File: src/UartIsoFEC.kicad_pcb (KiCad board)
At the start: 2 copper layers, 24 x 27.9 mm, 34 parts, among them J1 B3B-XH-A, P1 105444-0001, Q1 DMP3099L-13, U1 FT230XS, U2 ADUM5211

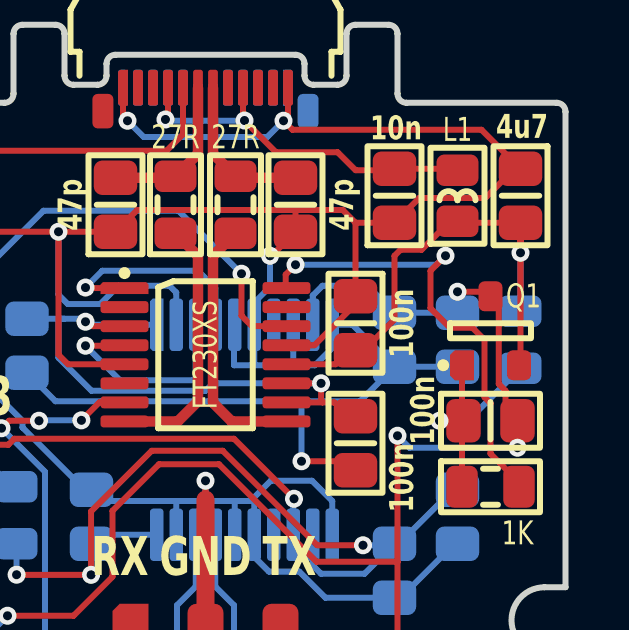
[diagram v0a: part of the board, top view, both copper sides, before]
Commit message: Minor cleanup and expanding soldermask
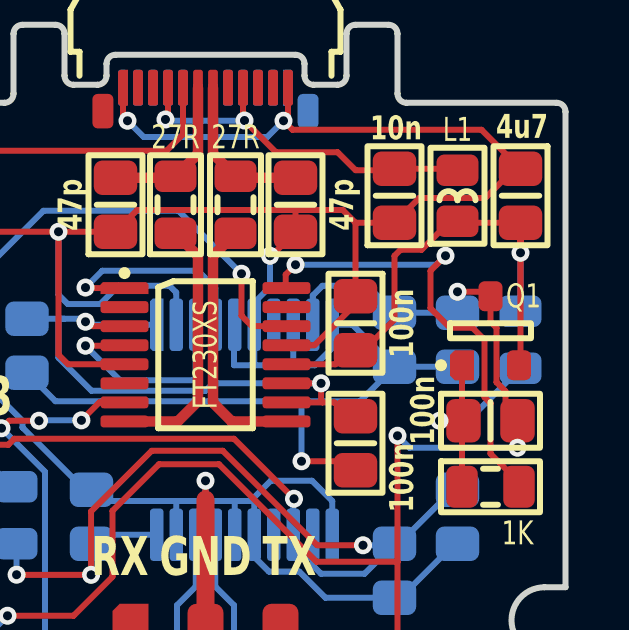
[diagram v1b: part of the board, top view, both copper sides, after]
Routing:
- net GND: track 94.2 -> 93.7 mm
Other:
- rule pad_to_mask_clearance: 0 -> 0.05
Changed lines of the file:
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@@
       (dielectric_constraints no)
     )
-    (pad_to_mask_clearance 0)
+    (pad_to_mask_clearance 0.05)
     (aux_axis_origin 20 20)
     (grid_origin 20 20)
@@
         (effects (font (size 0.8 0.6) (thickness 0.15)))
     )
+    (fp_text user "G" (at -0.95 0.5) (layer "Cmts.User" knockout)
+        (effects (font (size 0.13 0.07) (thickness 0.01) bold))
+    )
+    (fp_text user "D" (at 0 -0.5) (layer "Cmts.User" knockout)
+        (effects (font (size 0.13 0.07) (thickness 0.01) bold))
+    )
     (fp_text user "S" (at 0.95 0.5) (layer "Cmts.User" knockout)
         (effects (font (size 0.13 0.07) (thickness 0.01) bold))
     )
-    (fp_text user "G" (at -0.95 0.5) (layer "Cmts.User" knockout)
-        (effects (font (size 0.13 0.07) (thickness 0.01) bold))
-    )
-    (fp_text user "D" (at 0 -0.5) (layer "Cmts.User" knockout)
-        (effects (font (size 0.13 0.07) (thickness 0.01) bold))
-    )
     (fp_rect (start -1.35 -0.25) (end 1.35 0.25)
       (stroke (width 0.2) (type default)) (fill none) (layer "F.SilkS"))
-    (fp_circle (center -1.575 1.15) (end -1.425 1.15)
+    (fp_circle (center -1.65 1.15) (end -1.5 1.15)
       (stroke (width 0.1) (type solid)) (fill solid) (layer "F.SilkS"))
     (fp_rect (start -1.75 -1.95) (end 1.75 1.95)
@@
   (segment (start 29.4 23.2) (end 29.942136 23.742136) (width 0.2) (layer "B.Cu") (net 1))
   (segment (start 38.3 31.4) (end 40.4 31.4) (width 0.2) (layer "B.Cu") (net 1))
-  (segment (start 38.8 31.1) (end 38.3 31.1) (width 0.2) (layer "B.Cu") (net 1))
   (segment (start 28.48932 29.31068) (end 27.41068 29.31068) (width 0.2) (layer "B.Cu") (net 1))
   (segment (start 35.65 31.35) (end 36.225 30.775) (width 0.2) (layer "B.Cu") (net 1))
@@
   (segment (start 37.275 30.85) (end 38.3 29.825) (width 0.2) (layer "F.Cu") (net 8))
   (segment (start 38.3 29.825) (end 38.3 27.7) (width 0.2) (layer "F.Cu") (net 8))
-  (segment (start 40.15 26.55) (end 40.4 26.55) (width 0.2) (layer "F.Cu") (net 8))
   (segment (start 36.3325 31.3175) (end 36.95 30.7) (width 0.2) (layer "F.Cu") (net 8))
   (segment (start 42.5 27.6) (end 42.5 26.6) (width 0.2) (layer "F.Cu") (net 8))
@@
   (segment (start 38.4 33.7) (end 38.4 37.9) (width 0.2) (layer "F.Cu") (net 9))
   (segment (start 38.4 37.9) (end 38.4 41.8) (width 0.2) (layer "F.Cu") (net 9))
+  (segment (start 41.7 30.1) (end 41.7 31.918198) (width 0.2) (layer "F.Cu") (net 9))
   (segment (start 25.4 39.7) (end 27.6 39.7) (width 0.2) (layer "F.Cu") (net 9))
+  (segment (start 41.5 29.05) (end 41.5 29.9) (width 0.2) (layer "F.Cu") (net 9))
+  (segment (start 41.7 31.918198) (end 42 32.218198) (width 0.2) (layer "F.Cu") (net 9))
   (segment (start 41.35 28.9) (end 40.4 28.9) (width 0.2) (layer "F.Cu") (net 9))
   (segment (start 27.6 39.7) (end 28.9 38.4) (width 0.2) (layer "F.Cu") (net 9))
   (segment (start 42.4 33.2) (end 42.4 34.1) (width 0.2) (layer "F.Cu") (net 9))
+  (segment (start 41.5 29.9) (end 41.7 30.1) (width 0.2) (layer "F.Cu") (net 9))
   (segment (start 28.9 38.4) (end 28.9 36.2) (width 0.2) (layer "F.Cu") (net 9))
   (segment (start 38.4 41.8) (end 39.4 42.8) (width 0.2) (layer "F.Cu") (net 9))
-  (segment (start 41.775 29.325) (end 41.775 31.975) (width 0.2) (layer "F.Cu") (net 9))
+  (segment (start 42 32.218198) (end 42 32.8) (width 0.2) (layer "F.Cu") (net 9))
   (segment (start 35.7 37.9) (end 38.4 37.9) (width 0.2) (layer "F.Cu") (net 9))
-  (segment (start 42 32.2) (end 42 32.8) (width 0.2) (layer "F.Cu") (net 9))
   (segment (start 30.45 34.65) (end 32.45 34.65) (width 0.2) (layer "F.Cu") (net 9))
   (segment (start 32.45 34.65) (end 35.7 37.9) (width 0.2) (layer "F.Cu") (net 9))
-  (segment (start 41.5 29.05) (end 41.35 28.9) (width 0.2) (layer "F.Cu") (net 9))
-  (segment (start 41.775 31.975) (end 42 32.2) (width 0.2) (layer "F.Cu") (net 9))
   (via (at 42.4 34.1) (size 0.6) (drill 0.3) (layers "F.Cu" "B.Cu") (net 9))
   (via (at 25.4 39.7) (size 0.6) (drill 0.3) (layers "F.Cu" "B.Cu") (net 9))

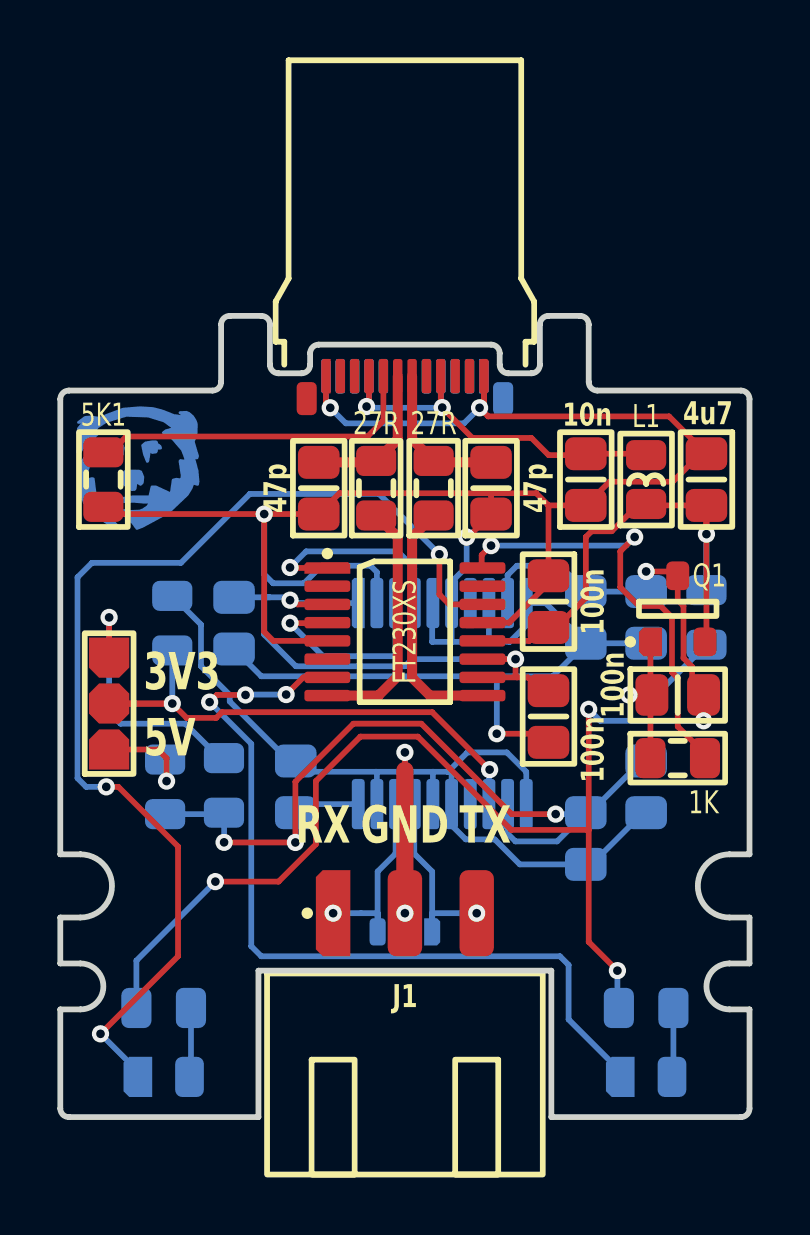
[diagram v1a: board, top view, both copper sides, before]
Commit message: Moved LEDs
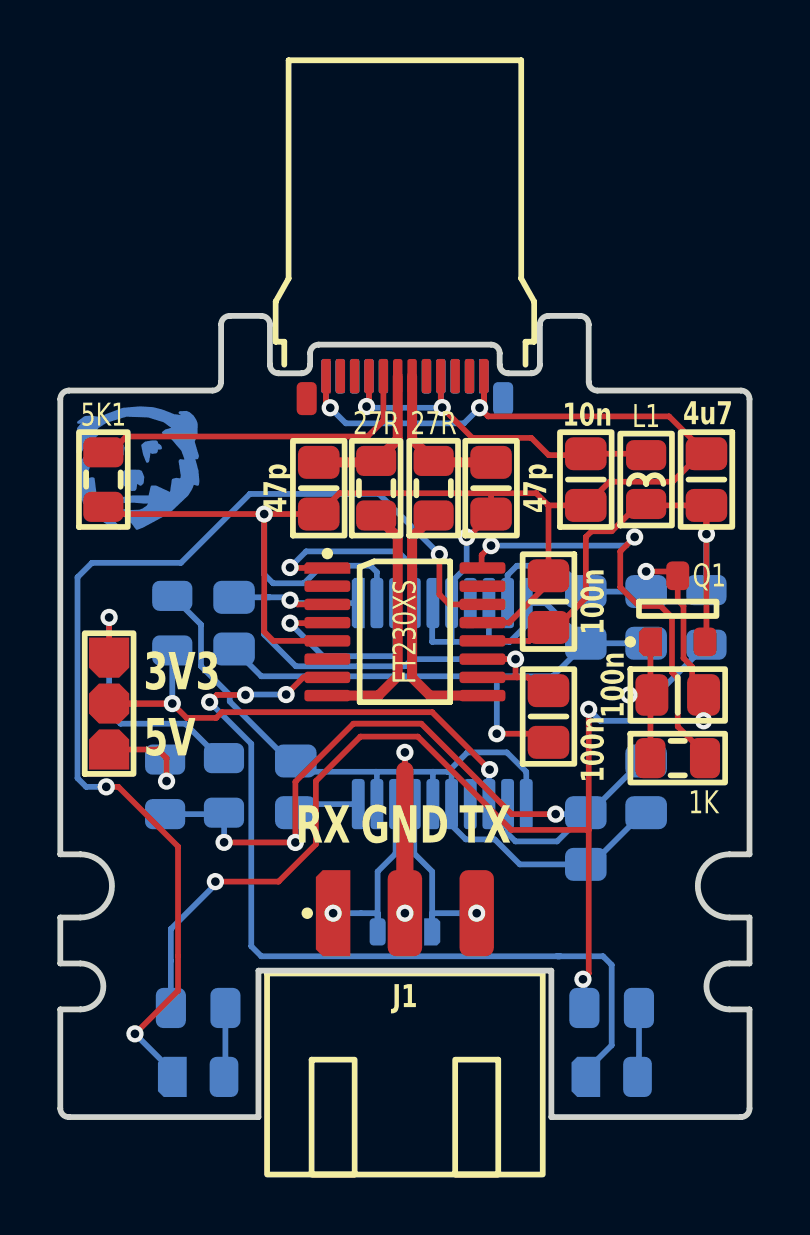
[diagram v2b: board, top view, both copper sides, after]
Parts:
- moved DS1 1.20 mm to (24.8, 46.5)
- moved R3 1.20 mm to (24.8, 44.1)
- moved DS2 1.20 mm to (39.2, 46.5)
- moved R4 1.20 mm to (39.2, 44.1)
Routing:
- net LED_TX: track 29.3 -> 30.8 mm
- net 5V_SWITCHED: track 50.6 -> 49.8 mm
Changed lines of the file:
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@@
   )
   (footprint "Medo64:R (0805)" (layer "B.Cu")
-    (at 40.4 44.1)
+    (at 39.2 44.1)
     (tags "RESC2013X70N")
     (attr smd)
@@
   )
   (footprint "Medo64:DS (0805)" (layer "B.Cu")
-    (at 40.4 46.5)
+    (at 39.2 46.5)
     (descr "LEDC2013X120N")
     (attr smd)
@@
   )
   (footprint "Medo64:DS (0805)" (layer "B.Cu")
-    (at 23.6 46.5)
+    (at 24.8 46.5)
     (descr "LEDC2013X120N")
     (attr smd)
@@
   )
   (footprint "Medo64:R (0805)" (layer "B.Cu")
-    (at 23.6 44.1)
+    (at 24.8 44.1)
     (tags "RESC2013X70N")
     (attr smd)
@@
   (via (at 42.5 27.6) (size 0.6) (drill 0.3) (layers "F.Cu" "B.Cu") (net 8))
   (segment (start 42.5 29.55) (end 42.5 27.6) (width 0.2) (layer "B.Cu") (net 8))
+  (segment (start 38.4 37.9) (end 38.4 42.9) (width 0.2) (layer "F.Cu") (net 9))
   (segment (start 28.9 36.2) (end 30.45 34.65) (width 0.2) (layer "F.Cu") (net 9))
   (segment (start 38.4 33.7) (end 38.4 37.9) (width 0.2) (layer "F.Cu") (net 9))
-  (segment (start 38.4 37.9) (end 38.4 41.8) (width 0.2) (layer "F.Cu") (net 9))
   (segment (start 41.7 30.1) (end 41.7 31.918198) (width 0.2) (layer "F.Cu") (net 9))
   (segment (start 25.4 39.7) (end 27.6 39.7) (width 0.2) (layer "F.Cu") (net 9))
@@
   (segment (start 41.7 31.918198) (end 42 32.218198) (width 0.2) (layer "F.Cu") (net 9))
   (segment (start 41.35 28.9) (end 40.4 28.9) (width 0.2) (layer "F.Cu") (net 9))
+  (segment (start 38.4 42.9) (end 38.2 43.1) (width 0.2) (layer "F.Cu") (net 9))
   (segment (start 27.6 39.7) (end 28.9 38.4) (width 0.2) (layer "F.Cu") (net 9))
   (segment (start 42.4 33.2) (end 42.4 34.1) (width 0.2) (layer "F.Cu") (net 9))
   (segment (start 41.5 29.9) (end 41.7 30.1) (width 0.2) (layer "F.Cu") (net 9))
   (segment (start 28.9 38.4) (end 28.9 36.2) (width 0.2) (layer "F.Cu") (net 9))
-  (segment (start 38.4 41.8) (end 39.4 42.8) (width 0.2) (layer "F.Cu") (net 9))
   (segment (start 42 32.218198) (end 42 32.8) (width 0.2) (layer "F.Cu") (net 9))
   (segment (start 35.7 37.9) (end 38.4 37.9) (width 0.2) (layer "F.Cu") (net 9))
@@
   (via (at 25.4 39.7) (size 0.6) (drill 0.3) (layers "F.Cu" "B.Cu") (net 9))
   (via (at 38.4 33.7) (size 0.6) (drill 0.3) (layers "F.Cu" "B.Cu") (net 9))
-  (via (at 39.4 42.8) (size 0.6) (drill 0.3) (layers "F.Cu" "B.Cu") (net 9))
+  (via (at 38.2 43.1) (size 0.6) (drill 0.3) (layers "F.Cu" "B.Cu") (net 9))
   (via (at 40.4 28.9) (size 0.6) (drill 0.3) (layers "F.Cu" "B.Cu") (net 9))
   (segment (start 40.6 29.1) (end 40.4 28.9) (width 0.2) (layer "B.Cu") (net 9))
   (segment (start 35.9 28.7) (end 37.4 28.7) (width 0.2) (layer "B.Cu") (net 9))
-  (segment (start 22.65 44.1) (end 22.65 42.45) (width 0.2) (layer "B.Cu") (net 9))
+  (segment (start 38.25 44.1) (end 38.25 43.15) (width 0.2) (layer "B.Cu") (net 9))
+  (segment (start 23.85 44.1) (end 23.85 42.45) (width 0.2) (layer "B.Cu") (net 9))
   (segment (start 37.4 28.7) (end 38.3 29.6) (width 0.2) (layer "B.Cu") (net 9))
+  (segment (start 38.25 43.15) (end 38.2 43.1) (width 0.2) (layer "B.Cu") (net 9))
   (segment (start 38.3 29.6) (end 40.4 29.6) (width 0.2) (layer "B.Cu") (net 9))
   (segment (start 35.575 29.025) (end 35.9 28.7) (width 0.2) (layer "B.Cu") (net 9))
+  (segment (start 23.85 42.45) (end 23.85 41.35) (width 0.2) (layer "B.Cu") (net 9))
   (segment (start 35.575 29.262348) (end 35.575 29.025) (width 0.2) (layer "B.Cu") (net 9))
   (segment (start 40.4 28.9) (end 40.4 29.6) (width 0.2) (layer "B.Cu") (net 9))
   (segment (start 38.8 34.1) (end 38.4 33.7) (width 0.2) (layer "B.Cu") (net 9))
-  (segment (start 39.4 42.8) (end 39.4 44.05) (width 0.2) (layer "B.Cu") (net 9))
-  (segment (start 22.65 42.45) (end 25.4 39.7) (width 0.2) (layer "B.Cu") (net 9))
+  (segment (start 23.85 41.35) (end 25.5 39.7) (width 0.2) (layer "B.Cu") (net 9))
   (segment (start 42.4 34.1) (end 38.8 34.1) (width 0.2) (layer "B.Cu") (net 9))
   (segment (start 40.55 35.4) (end 40.55 33.25) (width 0.2) (layer "F.Cu") (net 10))
@@
   (segment (start 31.675 38.725) (end 31.05 39.35) (width 0.2) (layer "B.Cu") (net 15))
   (segment (start 31.05 40.800056) (end 31.05 41.375) (width 0.2) (layer "B.Cu") (net 15))
-  (segment (start 41.35 44.1) (end 41.35 46.45) (width 0.2) (layer "B.Cu") (net 16))
+  (segment (start 40.15 44.1) (end 40.15 46.45) (width 0.2) (layer "B.Cu") (net 16))
   (segment (start 25.45 33.2) (end 25.2 33.45) (width 0.2) (layer "F.Cu") (net 17))
   (segment (start 28.4625 32.5875) (end 27.863909 33.186091) (width 0.2) (layer "F.Cu") (net 17))
@@
   (via (at 25.2 33.449998) (size 0.6) (drill 0.3) (layers "F.Cu" "B.Cu") (net 17))
   (via (at 26.45 33.2) (size 0.6) (drill 0.3) (layers "F.Cu" "B.Cu") (net 17))
-  (segment (start 39.5 46.3) (end 37.7 44.5) (width 0.2) (layer "B.Cu") (net 17))
+  (segment (start 39.2 42.6) (end 38.9 42.3) (width 0.2) (layer "B.Cu") (net 17))
+  (segment (start 26.65 34.9) (end 25.2 33.45) (width 0.2) (layer "B.Cu") (net 17))
+  (segment (start 37.4 42.3) (end 37.3 42.3) (width 0.2) (layer "B.Cu") (net 17))
+  (segment (start 26.463909 33.186091) (end 26.45 33.2) (width 0.2) (layer "B.Cu") (net 17))
   (segment (start 26.65 41.95) (end 26.65 34.9) (width 0.2) (layer "B.Cu") (net 17))
-  (segment (start 37.7 44.5) (end 37.7 42.6) (width 0.2) (layer "B.Cu") (net 17))
+  (segment (start 39.2 45.4) (end 39.2 42.6) (width 0.2) (layer "B.Cu") (net 17))
+  (segment (start 27.863909 33.186091) (end 26.463909 33.186091) (width 0.2) (layer "B.Cu") (net 17))
+  (segment (start 38.3 46.5) (end 38.3 46.3) (width 0.2) (layer "B.Cu") (net 17))
+  (segment (start 37.4 42.3) (end 27 42.3) (width 0.2) (layer "B.Cu") (net 17))
+  (segment (start 38.9 42.3) (end 37.3 42.3) (width 0.2) (layer "B.Cu") (net 17))
+  (segment (start 38.3 46.3) (end 39.2 45.4) (width 0.2) (layer "B.Cu") (net 17))
   (segment (start 27 42.3) (end 26.65 41.95) (width 0.2) (layer "B.Cu") (net 17))
-  (segment (start 26.463909 33.186091) (end 26.45 33.2) (width 0.2) (layer "B.Cu") (net 17))
-  (segment (start 26.65 34.9) (end 25.2 33.45) (width 0.2) (layer "B.Cu") (net 17))
-  (segment (start 37.4 42.3) (end 27 42.3) (width 0.2) (layer "B.Cu") (net 17))
-  (segment (start 27.863909 33.186091) (end 26.463909 33.186091) (width 0.2) (layer "B.Cu") (net 17))
-  (segment (start 37.7 42.6) (end 37.4 42.3) (width 0.2) (layer "B.Cu") (net 17))
-  (segment (start 24.1 42.29999) (end 21.399995 44.999995) (width 0.2) (layer "F.Cu") (net 18))
+  (segment (start 24.1 43.49999) (end 22.599995 44.999995) (width 0.2) (layer "F.Cu") (net 18))
   (segment (start 33.2 29.7) (end 33.2 28.3) (width 0.2) (layer "F.Cu") (net 18))
   (segment (start 21.6 36.4) (end 22.022182 36.4) (width 0.2) (layer "F.Cu") (net 18))
   (segment (start 22.022182 36.4) (end 24.1 38.477818) (width 0.2) (layer "F.Cu") (net 18))
   (segment (start 34.7 30.0475) (end 33.5475 30.0475) (width 0.2) (layer "F.Cu") (net 18))
+  (segment (start 24.1 42.29999) (end 24.1 43.49999) (width 0.2) (layer "F.Cu") (net 18))
   (segment (start 24.1 38.477818) (end 24.1 42.29999) (width 0.2) (layer "F.Cu") (net 18))
   (segment (start 33.5475 30.0475) (end 33.2 29.7) (width 0.2) (layer "F.Cu") (net 18))
   (via (at 33.2 28.3) (size 0.6) (drill 0.3) (layers "F.Cu" "B.Cu") (net 18))
   (via (at 21.6 36.4) (size 0.6) (drill 0.3) (layers "F.Cu" "B.Cu") (net 18))
-  (via (at 21.399995 44.999995) (size 0.6) (drill 0.3) (layers "F.Cu" "B.Cu") (net 18))
+  (via (at 22.599994 44.999996) (size 0.6) (drill 0.3) (layers "F.Cu" "B.Cu") (net 18))
   (segment (start 31.1 26.2) (end 26.6 26.2) (width 0.2) (layer "B.Cu") (net 18))
   (segment (start 21.1 28.6) (end 20.598939 29.101061) (width 0.2) (layer "B.Cu") (net 18))
@@
   (segment (start 20.9 36.4) (end 21.6 36.4) (width 0.2) (layer "B.Cu") (net 18))
   (segment (start 20.598939 36.098939) (end 20.9 36.4) (width 0.2) (layer "B.Cu") (net 18))
-  (segment (start 22.7 46.3) (end 21.399995 44.999995) (width 0.2) (layer "B.Cu") (net 18))
+  (segment (start 23.9 46.3) (end 22.599995 44.999995) (width 0.2) (layer "B.Cu") (net 18))
   (segment (start 24.2 28.6) (end 21.1 28.6) (width 0.2) (layer "B.Cu") (net 18))
   (segment (start 26.6 26.2) (end 24.2 28.6) (width 0.2) (layer "B.Cu") (net 18))
-  (segment (start 24.55 46.45) (end 24.55 44.1) (width 0.2) (layer "B.Cu") (net 19))
+  (segment (start 25.75 46.45) (end 25.75 44.1) (width 0.2) (layer "B.Cu") (net 19))
   (segment (start 21.7 33.5) (end 23.9 33.5) (width 0.2) (layer "F.Cu") (net 20))
   (segment (start 25.627816 33.8) (end 32.95 33.8) (width 0.2) (layer "F.Cu") (net 20))
